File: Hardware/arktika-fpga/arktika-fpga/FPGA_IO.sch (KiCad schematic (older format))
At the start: 10 parts

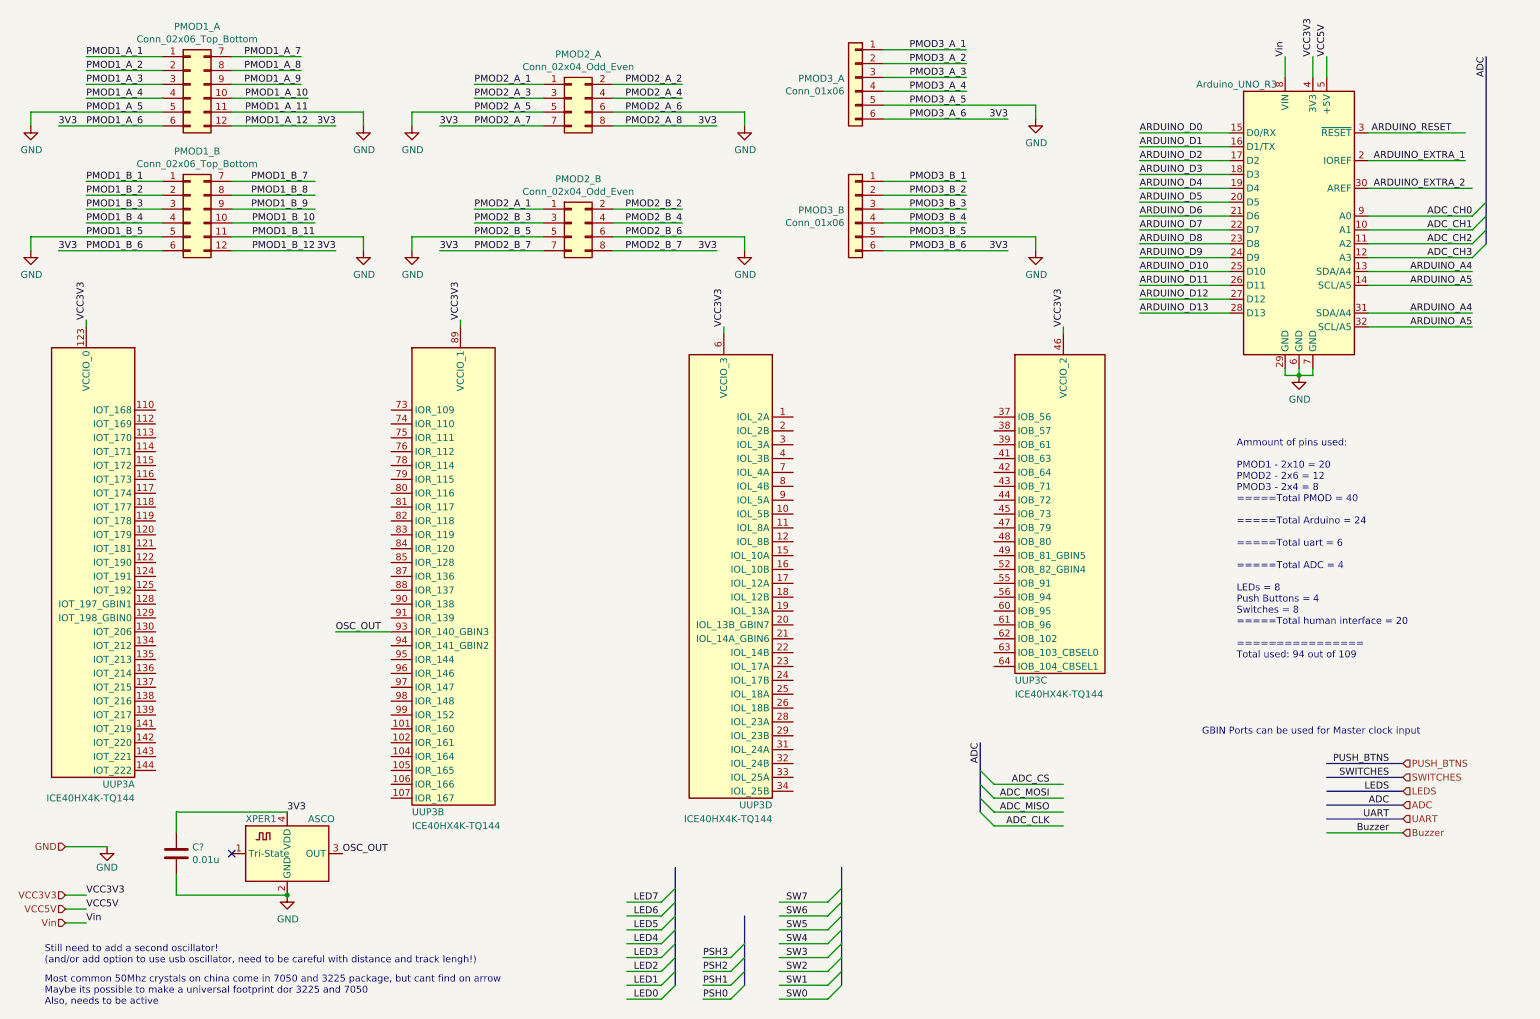
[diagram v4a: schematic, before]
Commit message: Addded new hybrid crystal footprint, fixed missing footprints, created layout file for testing
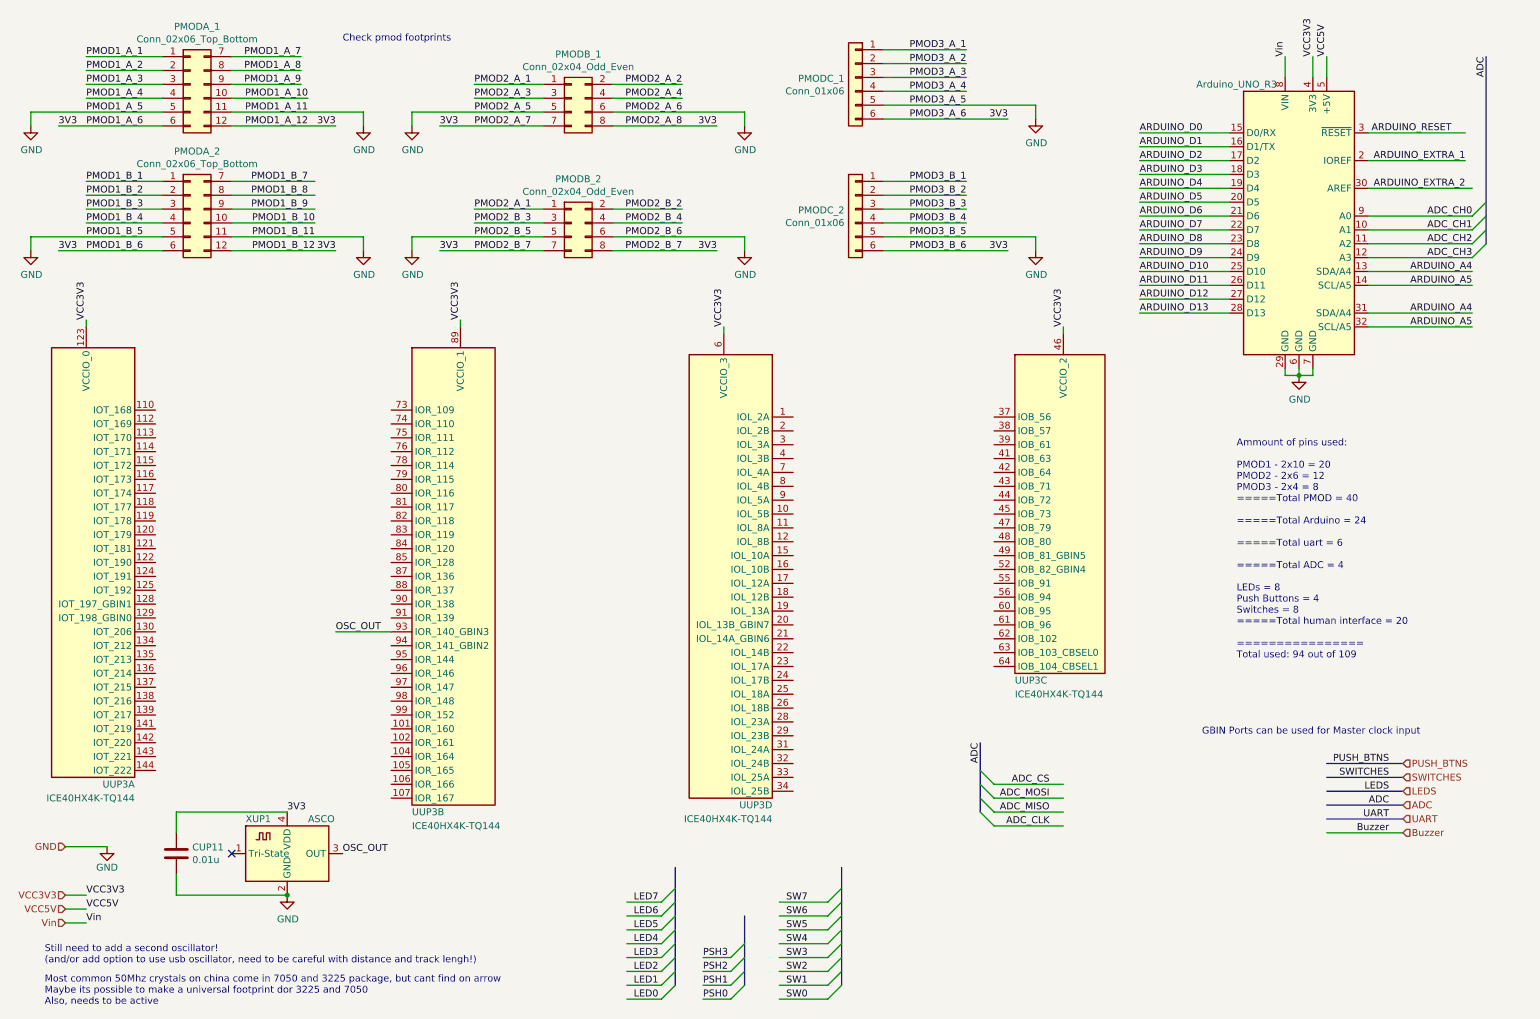
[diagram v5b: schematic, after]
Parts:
- A1: footprint Module:Arduino_UNO_R3 -> Modules:Arduino_UNO_R3
- CUP11: renamed from C?; footprint (none) -> Capacitors_SMD:C_0603_HandSoldering
- PMODA_1: renamed from PMOD1_A; footprint (none) -> Pin_Headers:Pin_Header_Angled_2x06_Pitch2.54mm
- PMODA_2: renamed from PMOD1_B; footprint (none) -> Pin_Headers:Pin_Header_Angled_2x06_Pitch2.54mm
- PMODB_1: renamed from PMOD2_A; footprint (none) -> Pin_Headers:Pin_Header_Angled_2x04_Pitch2.54mm
- PMODB_2: renamed from PMOD2_B; footprint (none) -> Pin_Headers:Pin_Header_Angled_2x04_Pitch2.54mm
- PMODC_1: renamed from PMOD3_A; footprint (none) -> Pin_Headers:Pin_Header_Angled_1x06_Pitch2.54mm
- PMODC_2: renamed from PMOD3_B; footprint (none) -> Pin_Headers:Pin_Header_Angled_1x06_Pitch2.54mm
- UUP3: footprint Package_QFP:TQFP-144_20x20mm_P0.5mm -> Housings_QFP:TQFP-144_20x20mm_Pitch0.5mm
- XUP1: renamed from XPER1; footprint Crystals:Crystal_SMD_3225-4pin_3.2x2.5mm_HandSoldering -> Arktica-Specific:Crystal_SMD_7050-4pin_7.0x5.0mm_MOD_3225
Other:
- note added: "Check pmod footprints\n"
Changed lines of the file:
@@
 F 0 "UUP3" H 700 3050 50  0000 L CNN
 F 1 "ICE40HX4K-TQ144" H 700 2950 50  0000 L CNN
-F 2 "Package_QFP:TQFP-144_20x20mm_P0.5mm" H 2050 2650 50  0001 R CNN
+F 2 "Housings_QFP:TQFP-144_20x20mm_Pitch0.5mm" H 2050 2650 50  0001 R CNN
 F 3 "http://www.latticesemi.com/Products/FPGAandCPLD/iCE40" H 50  7050 50  0001 C CNN
 	1    1050 4550
@@
 F 0 "UUP3" H 3400 3050 50  0000 L CNN
 F 1 "ICE40HX4K-TQ144" H 3400 2950 50  0000 L CNN
-F 2 "Package_QFP:TQFP-144_20x20mm_P0.5mm" H 4750 2750 50  0001 R CNN
+F 2 "Housings_QFP:TQFP-144_20x20mm_Pitch0.5mm" H 4750 2750 50  0001 R CNN
 F 3 "http://www.latticesemi.com/Products/FPGAandCPLD/iCE40" H 2750 7150 50  0001 C CNN
 	2    3750 4650
@@
 F 0 "UUP3" H 7750 3100 50  0000 L CNN
 F 1 "ICE40HX4K-TQ144" H 7750 3000 50  0000 L CNN
-F 2 "Package_QFP:TQFP-144_20x20mm_P0.5mm" H 9100 2300 50  0001 R CNN
+F 2 "Housings_QFP:TQFP-144_20x20mm_Pitch0.5mm" H 9100 2300 50  0001 R CNN
 F 3 "http://www.latticesemi.com/Products/FPGAandCPLD/iCE40" H 7100 6700 50  0001 C CNN
 	3    8100 4200
@@
 F 0 "UUP3" H 5300 3000 50  0000 L CNN
 F 1 "ICE40HX4K-TQ144" H 5300 2900 50  0000 L CNN
-F 2 "Package_QFP:TQFP-144_20x20mm_P0.5mm" H 6650 2700 50  0001 R CNN
+F 2 "Housings_QFP:TQFP-144_20x20mm_Pitch0.5mm" H 6650 2700 50  0001 R CNN
 F 3 "http://www.latticesemi.com/Products/FPGAandCPLD/iCE40" H 4650 7100 50  0001 C CNN
 	4    5650 4600
@@
 $EndComp
 $Comp
-L Connector_Generic:Conn_02x06_Top_Bottom PMOD1_A
+L Connector_Generic:Conn_02x06_Top_Bottom PMODA_1
 U 1 1 5F5824E2
 P 1800 1000
-F 0 "PMOD1_A" H 1850 1417 50  0000 C CNN
+F 0 "PMODA_1" H 1850 1417 50  0000 C CNN
 F 1 "Conn_02x06_Top_Bottom" H 1850 1326 50  0000 C CNN
-F 2 "" H 1800 1000 50  0001 C CNN
+F 2 "Pin_Headers:Pin_Header_Angled_2x06_Pitch2.54mm" H 1800 1000 50  0001 C CNN
 F 3 "~" H 1800 1000 50  0001 C CNN
 	1    1800 1000
@@
 $EndComp
 $Comp
-L Connector_Generic:Conn_02x06_Top_Bottom PMOD1_B
+L Connector_Generic:Conn_02x06_Top_Bottom PMODA_2
 U 1 1 5F5844DB
 P 1800 1900
-F 0 "PMOD1_B" H 1850 2317 50  0000 C CNN
+F 0 "PMODA_2" H 1850 2317 50  0000 C CNN
 F 1 "Conn_02x06_Top_Bottom" H 1850 2226 50  0000 C CNN
-F 2 "" H 1800 1900 50  0001 C CNN
+F 2 "Pin_Headers:Pin_Header_Angled_2x06_Pitch2.54mm" H 1800 1900 50  0001 C CNN
 F 3 "~" H 1800 1900 50  0001 C CNN
 	1    1800 1900
@@
 $EndComp
 $Comp
-L Connector_Generic:Conn_02x04_Odd_Even PMOD2_A
+L Connector_Generic:Conn_02x04_Odd_Even PMODB_1
 U 1 1 5F586835
 P 4550 1100
-F 0 "PMOD2_A" H 4600 1417 50  0000 C CNN
+F 0 "PMODB_1" H 4600 1417 50  0000 C CNN
 F 1 "Conn_02x04_Odd_Even" H 4600 1326 50  0000 C CNN
-F 2 "" H 4550 1100 50  0001 C CNN
+F 2 "Pin_Headers:Pin_Header_Angled_2x04_Pitch2.54mm" H 4550 1100 50  0001 C CNN
 F 3 "~" H 4550 1100 50  0001 C CNN
 	1    4550 1100
@@
 $EndComp
 $Comp
-L Connector_Generic:Conn_02x04_Odd_Even PMOD2_B
+L Connector_Generic:Conn_02x04_Odd_Even PMODB_2
 U 1 1 5F5882E5
 P 4550 2000
-F 0 "PMOD2_B" H 4600 2317 50  0000 C CNN
+F 0 "PMODB_2" H 4600 2317 50  0000 C CNN
 F 1 "Conn_02x04_Odd_Even" H 4600 2226 50  0000 C CNN
-F 2 "" H 4550 2000 50  0001 C CNN
+F 2 "Pin_Headers:Pin_Header_Angled_2x04_Pitch2.54mm" H 4550 2000 50  0001 C CNN
 F 3 "~" H 4550 2000 50  0001 C CNN
 	1    4550 2000
@@
 $EndComp
 $Comp
-L Connector_Generic:Conn_01x06 PMOD3_A
+L Connector_Generic:Conn_01x06 PMODC_1
 U 1 1 5F58A547
 P 6600 950
-F 0 "PMOD3_A" H 6680 942 50  0000 L CNN
+F 0 "PMODC_1" H 6680 942 50  0000 L CNN
 F 1 "Conn_01x06" H 6680 851 50  0000 L CNN
-F 2 "" H 6600 950 50  0001 C CNN
+F 2 "Pin_Headers:Pin_Header_Angled_1x06_Pitch2.54mm" H 6600 950 50  0001 C CNN
 F 3 "~" H 6600 950 50  0001 C CNN
 	1    6600 950
@@
 $EndComp
 $Comp
-L Connector_Generic:Conn_01x06 PMOD3_B
+L Connector_Generic:Conn_01x06 PMODC_2
 U 1 1 5F58B5B0
 P 6600 1900
-F 0 "PMOD3_B" H 6680 1892 50  0000 L CNN
+F 0 "PMODC_2" H 6680 1892 50  0000 L CNN
 F 1 "Conn_01x06" H 6680 1801 50  0000 L CNN
-F 2 "" H 6600 1900 50  0001 C CNN
+F 2 "Pin_Headers:Pin_Header_Angled_1x06_Pitch2.54mm" H 6600 1900 50  0001 C CNN
 F 3 "~" H 6600 1900 50  0001 C CNN
 	1    6600 1900
@@
 F 0 "A1" H 8800 3150 50  0001 C CNN
 F 1 "Arduino_UNO_R3" H 9350 2900 50  0000 C CNN
-F 2 "Module:Arduino_UNO_R3" H 9800 1950 50  0001 C CIN
+F 2 "Modules:Arduino_UNO_R3" H 9800 1950 50  0001 C CIN
 F 3 "https://www.arduino.cc/en/Main/arduinoBoardUno" H 9800 1950 50  0001 C CNN
 	1    9800 1950
@@
 Most common 50Mhz crystals on china come in 7050 and 3225 package, but cant find on arrow\nMaybe its possible to make a universal footprint dor 3225 and 7050\nAlso, needs to be active
 $Comp
-L Oscillator:ASCO XPER1
+L Oscillator:ASCO XUP1
 U 1 1 5F23DFDD
 P 2500 6550
-F 0 "XPER1" H 2200 6800 50  0000 L CNN
+F 0 "XUP1" H 2200 6800 50  0000 L CNN
 F 1 "ASCO" H 2650 6800 50  0000 L CNN
-F 2 "Crystals:Crystal_SMD_3225-4pin_3.2x2.5mm_HandSoldering" H 2600 6200 50  0001 C CNN
+F 2 "Arktica-Specific:Crystal_SMD_7050-4pin_7.0x5.0mm_MOD_3225" H 2600 6200 50  0001 C CNN
 F 3 "https://abracon.com/Oscillators/ASCO.pdf" H 2275 6675 50  0001 C CNN
 	1    2500 6550
@@
 $EndComp
 $Comp
-L Device:C C?
+L Device:C CUP11
 U 1 1 5F23EF40
 P 1700 6550
-F 0 "C?" H 1815 6596 50  0000 L CNN
+F 0 "CUP11" H 1815 6596 50  0000 L CNN
 F 1 "0.01u" H 1815 6505 50  0000 L CNN
-F 2 "" H 1738 6400 50  0001 C CNN
+F 2 "Capacitors_SMD:C_0603_HandSoldering" H 1738 6400 50  0001 C CNN
 F 3 "~" H 1700 6550 50  0001 C CNN
 	1    1700 6550
@@
 Wire Bus Line
 	5300 6650 5300 7500
+Text Notes 2900 700  0    50   ~ 0
+Check pmod footprints\n
 $EndSCHEMATC

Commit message: Misc schematic changes. Preliminary layout almost complete
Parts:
- added JPUP6_2, JUP6_1: SolderJumper_2_Open, Jumper:SolderJumper-2_P1.3mm_Open_RoundedPad1.0x1.5mm, symbol Jumper:SolderJumper_2_Open
- A1: footprint Modules:Arduino_UNO_R3 -> Module:Arduino_UNO_R3_WithMountingHoles; symbol MCU_Module:Arduino_UNO_R3 -> arktika-fpga-rescue:Arduino_UNO_R3-MCU_Module
- CUP11: footprint Capacitors_SMD:C_0603_HandSoldering -> Capacitor_SMD:C_0603_1608Metric_Pad1.05x0.95mm_HandSolder; symbol Device:C -> arktika-fpga-rescue:C-Device
- PMODA_1, PMODA_2: footprint Pin_Headers:Pin_Header_Angled_2x06_Pitch2.54mm -> Connector_PinHeader_2.54mm:PinHeader_2x06_P2.54mm_Horizontal; symbol Connector_Generic:Conn_02x06_Top_Bottom -> arktika-fpga-rescue:Conn_02x06_Top_Bottom-Connector_Generic
- PMODB_1, PMODB_2: footprint Pin_Headers:Pin_Header_Angled_2x04_Pitch2.54mm -> Connector_PinHeader_2.54mm:PinHeader_2x04_P2.54mm_Horizontal; symbol Connector_Generic:Conn_02x04_Odd_Even -> arktika-fpga-rescue:Conn_02x04_Odd_Even-Connector_Generic
- PMODC_1, PMODC_2: footprint Pin_Headers:Pin_Header_Angled_1x06_Pitch2.54mm -> Connector_PinHeader_2.54mm:PinHeader_1x06_P2.54mm_Horizontal; symbol Connector_Generic:Conn_01x06 -> arktika-fpga-rescue:Conn_01x06-Connector_Generic
- UUP3: footprint Housings_QFP:TQFP-144_20x20mm_Pitch0.5mm -> Package_QFP:TQFP-144_20x20mm_P0.5mm; symbol FPGA_Lattice:ICE40HX4K-TQ144 -> arktika-fpga-rescue:ICE40HX4K-TQ144-FPGA_Lattice
- XUP1: symbol Oscillator:ASCO -> arktika-fpga-rescue:ASCO-Oscillator
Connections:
- net labels added: D+, D-, EXT1, LED[0..7], PSH[0..3], SW[0..7], UART_RX, UART_TX
- net labels removed: LEDS, PUSH_BTNS, SWITCHES, UART
- wire segments 133 -> 188

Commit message: Major routing updates. Did work on silkscreen. Optimized io placing. Misc changes
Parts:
- removed PMODA_1, PMODA_2: Conn_02x06_Top_Bottom, Connector_PinHeader_2.54mm:PinHeader_2x06_P2.54mm_Horizontal, symbol arktika-fpga-rescue:Conn_02x06_Top_Bottom-Connector_Generic
- added PMODA_1, PMODA_2: Conn_02x06_Odd_Even, Connector_PinHeader_2.54mm:PinHeader_2x06_P2.54mm_Horizontal, symbol Connector_Generic:Conn_02x06_Odd_Even
- A1: footprint Module:Arduino_UNO_R3_WithMountingHoles -> Module:Arduino_UNO_R3
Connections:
- net labels added: PMOD2_B_1
- net labels removed: 3V3, PMOD1_A_12, PMOD1_A_6, PMOD1_B_12, PMOD1_B_6, PMOD2_A_7, PMOD2_A_8, PMOD2_B_7, PMOD3_A_6, PMOD3_B_6
- wire segments 188 -> 190
